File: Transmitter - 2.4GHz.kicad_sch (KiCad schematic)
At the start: 0 parts

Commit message: added RF ransceiver
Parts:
- added C19: 10uF 16V, 0_capacitors:CP_EIA-3216-18_Kemet-A, symbol 0_capacitors:TAJA106K016RNJ
- added C20: 100nF, 0_capacitors:C_0402_1005Metric, symbol 0_capacitors:CL05B104KO5NNNC
- added C21: 4.7uF, 0_capacitors:C_0805_2012Metric, symbol 0_capacitors:CL21A475KAQNNNE
- added E01-2G4M27D1: DS1023-2*4SF11, 0_modules:PE01-ML01DP5, symbol 0_modules:AFC07-S10ECC-00
- added R13, R14: 10kΩ, 0_resistors:R_0402_1005Metric, symbol 0_resistors:0402WGF1002TCE
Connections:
- new net +3.3V: C19.1, C20.1, C21.1, E01-2G4M27D1.2 (VCC), R13.2, R14.2
- new net GND: C19.2, C20.2, C21.2, E01-2G4M27D1.1 (GND)
- new net RF_CE: E01-2G4M27D1.3 (CE)
- new net RF_IRQ: E01-2G4M27D1.8 (IRQ), R14.1
- new net SPI5_MISO: E01-2G4M27D1.7 (MISO)
- new net SPI5_MOSI: E01-2G4M27D1.6 (MOSI)
- new net SPI5_NSS: E01-2G4M27D1.4 (CSN), R13.1
- new net SPI5_SCK: E01-2G4M27D1.5 (SCK)
- no-connect marks 0 -> 1

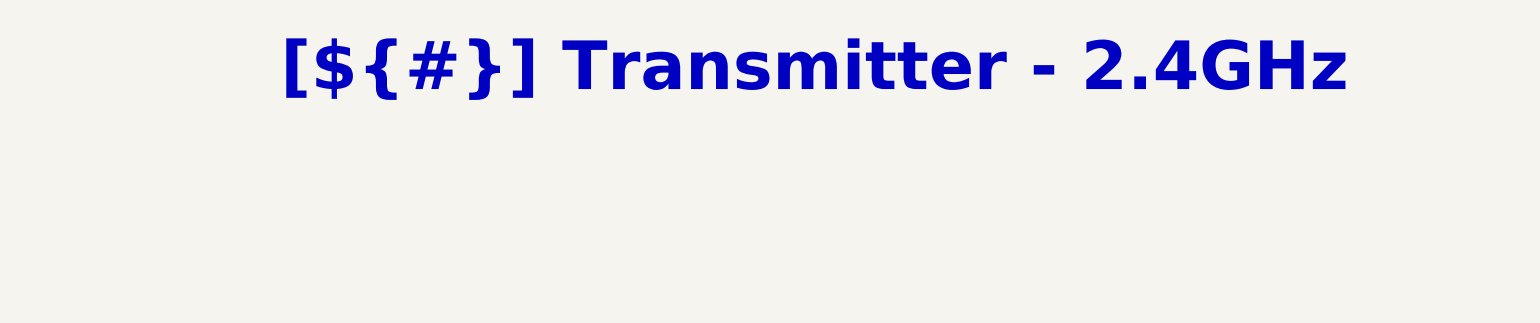
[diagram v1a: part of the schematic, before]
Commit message: added sd card schematic and refactor page numbers and general tab
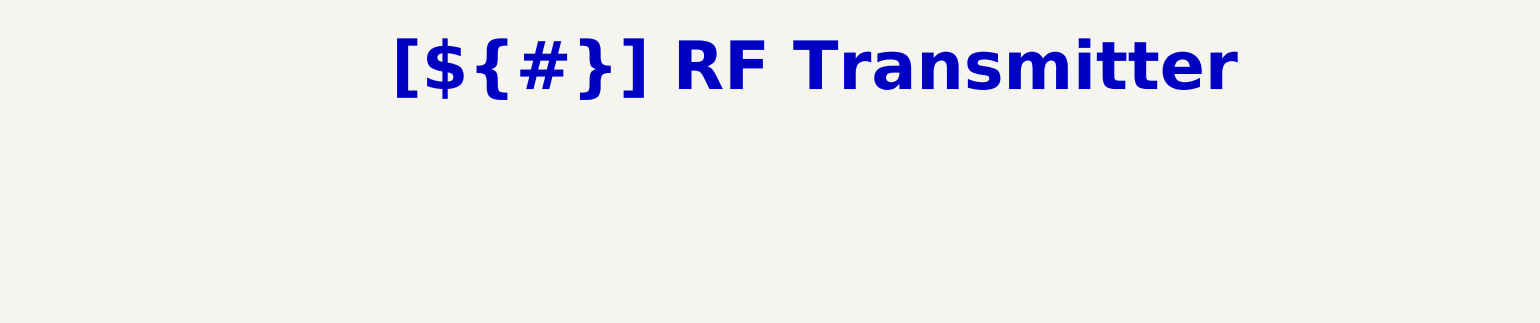
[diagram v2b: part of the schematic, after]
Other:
- title: Transmitter - 2.4GHz -> RF Transmitter
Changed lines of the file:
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@@
 	(paper "A3")
 	(title_block
-		(title "Transmitter - 2.4GHz")
+		(title "RF Transmitter")
 		(rev "${REVISION}")
 		(company "${COMPANY}")

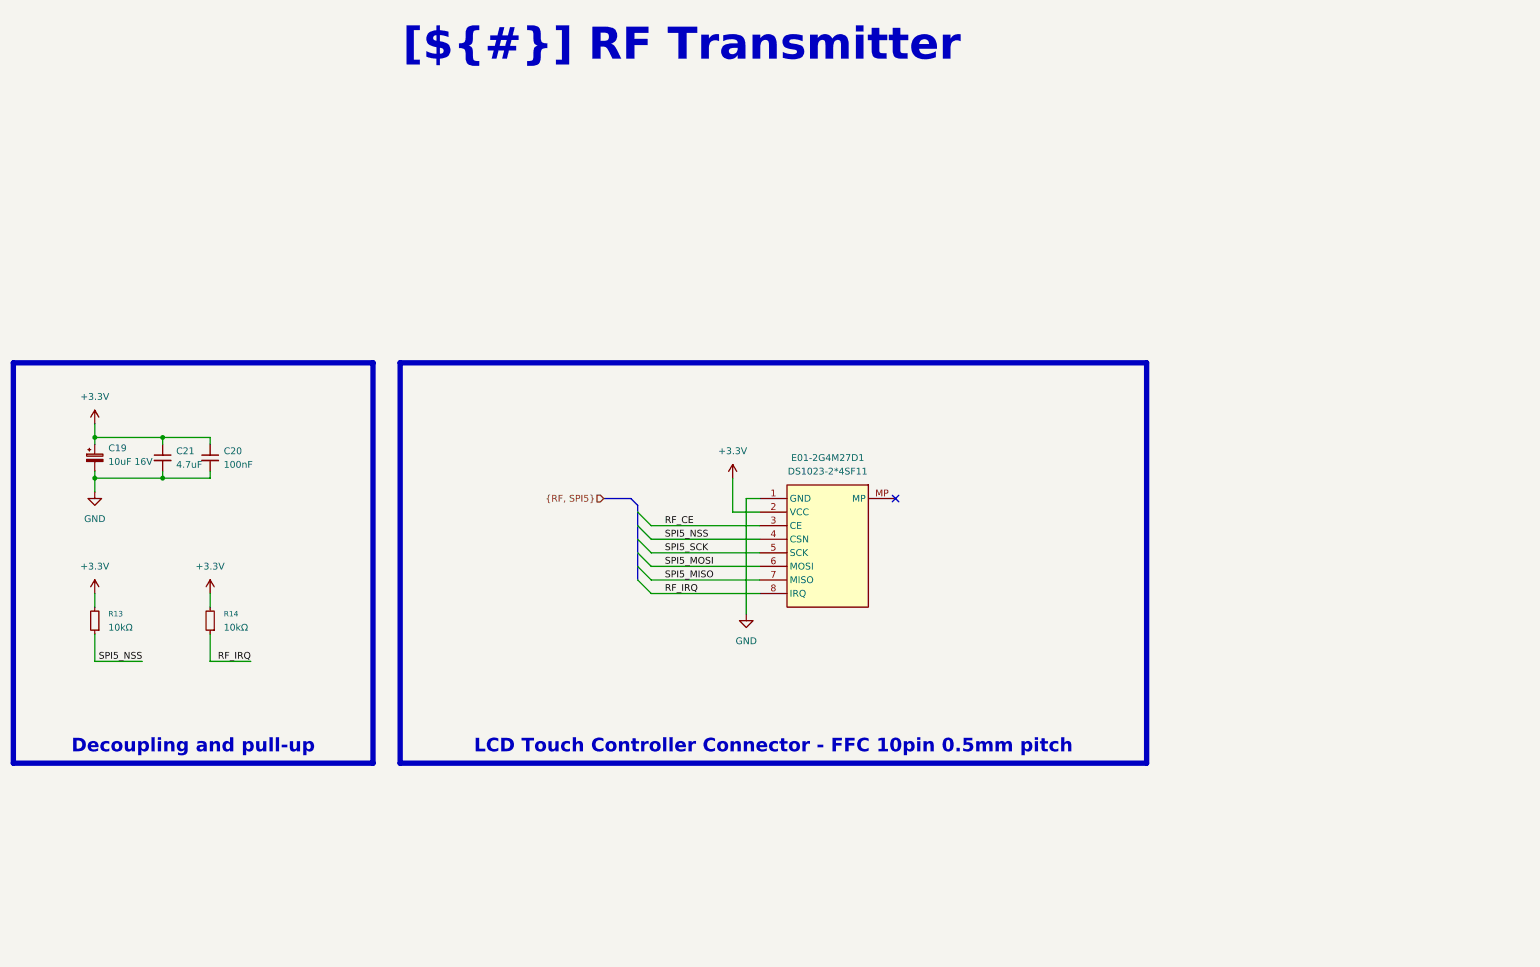
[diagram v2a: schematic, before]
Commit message: change the rf trasceiver and improve grounding near vias close to lcd connector
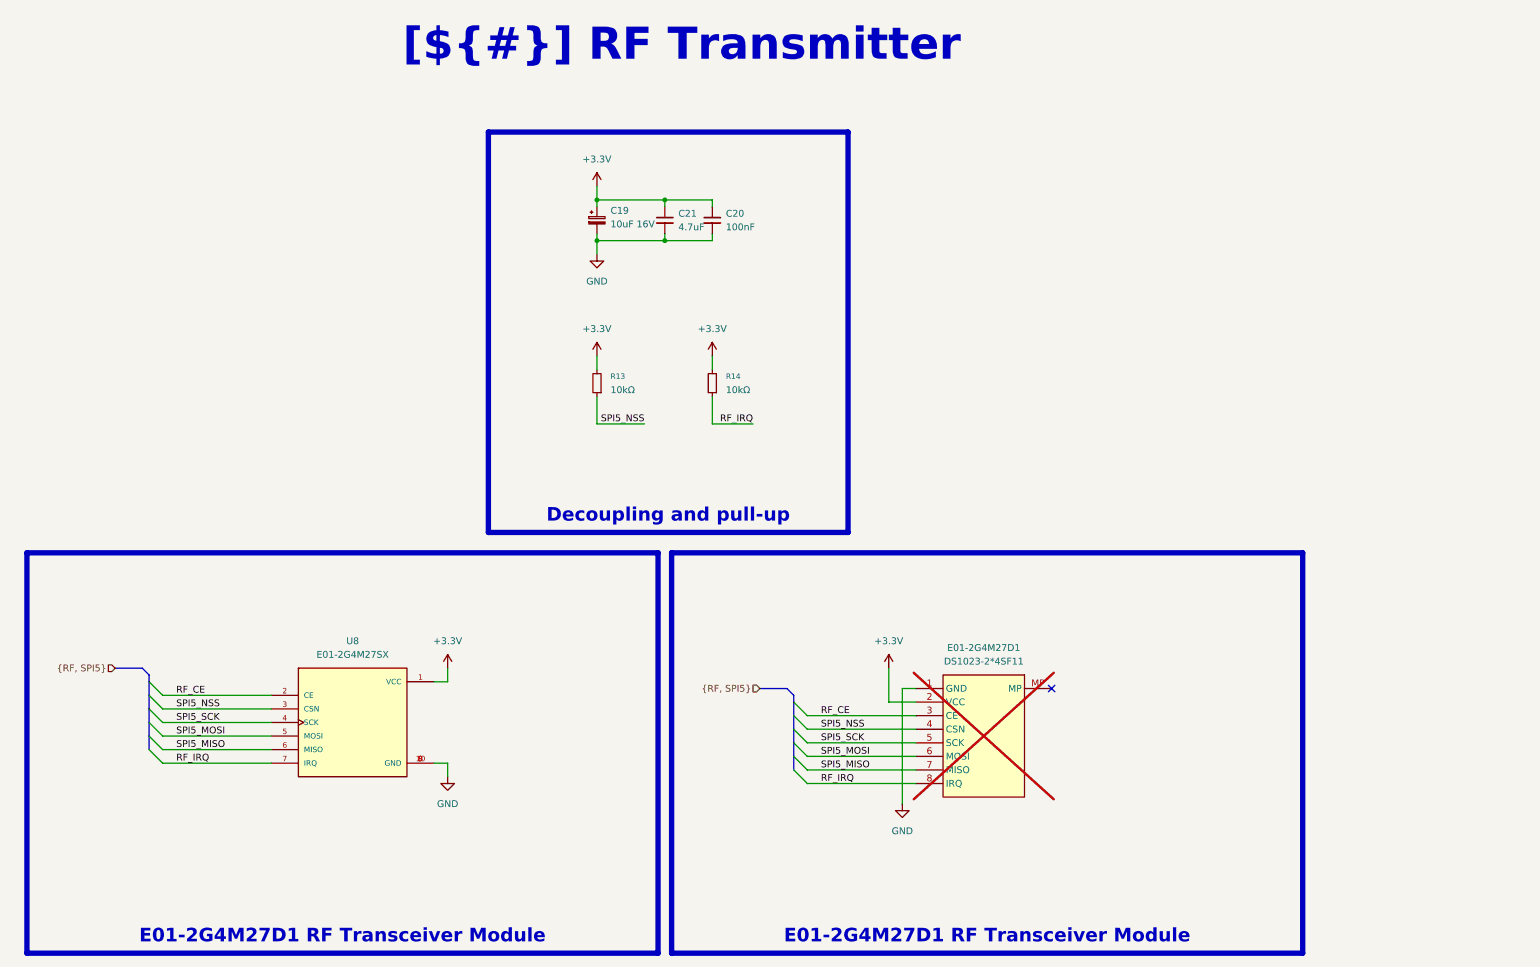
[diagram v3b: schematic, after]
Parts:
- added U8: E01-2G4M27SX, 0_modules:E01-2G4M27SX, symbol 0_modules:E01-2G4M27SX
- E01-2G4M27D1: now not fitted; now left out of the parts list
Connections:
- net +3.3V: now also U8.1 (VCC)
- net GND: now also U8.10 (GND), U8.8 (GND), U8.9 (GND)
- net RF_CE: now also U8.2 (CE)
- net RF_IRQ: now also U8.7 (IRQ)
- net SPI5_MISO: now also U8.6 (MISO)
- net SPI5_MOSI: now also U8.5 (MOSI)
- net SPI5_NSS: now also U8.3 (CSN)
- net SPI5_SCK: now also U8.4 (SCK)
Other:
- moved on the sheet: C19, C20, C21, R13, R14

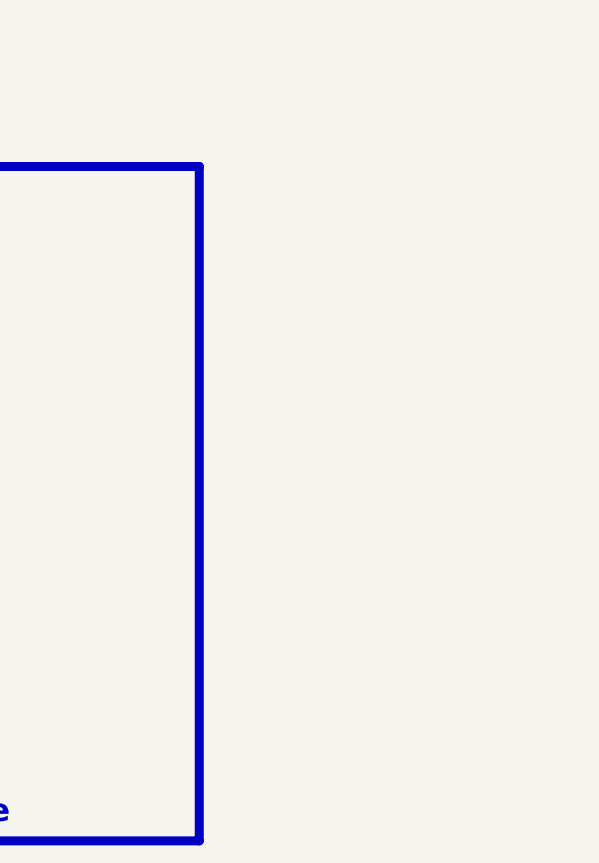
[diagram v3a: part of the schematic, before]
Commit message: added fiducal markers, mounting holes, testpoints
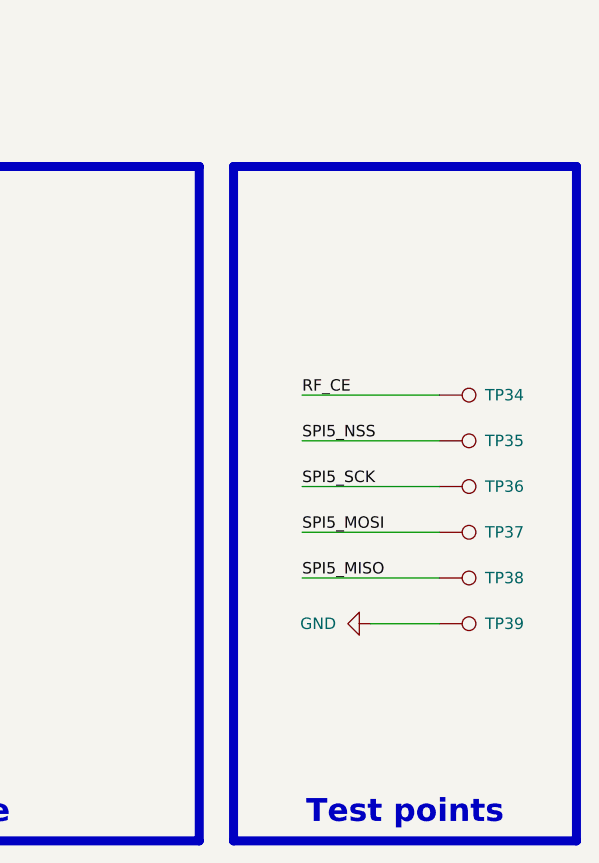
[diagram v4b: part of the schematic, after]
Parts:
- added TP34, TP35, TP36, TP37, TP38, TP39: TestPoint, 0_pads:TestPoint_Pad_D0.4mm_Back, symbol Connector:TestPoint
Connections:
- net GND: now also TP39.1
- net RF_CE: now also TP34.1
- net SPI5_MISO: now also TP38.1
- net SPI5_MOSI: now also TP37.1
- net SPI5_NSS: now also TP35.1
- net SPI5_SCK: now also TP36.1

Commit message: test points, colors, drc
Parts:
- TP34, TP35, TP36, TP37, TP38, TP39: footprint 0_pads:TestPoint_Pad_D0.4mm_Back -> 0_pads:TestPoint_Pad_D0.5mm_Back
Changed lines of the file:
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@@
 			)
 		)
-		(property "Footprint" "0_pads:TestPoint_Pad_D0.4mm_Back"
+		(property "Footprint" "0_pads:TestPoint_Pad_D0.5mm_Back"
 			(at 353.06 149.86 0)
 			(effects
@@
 			)
 		)
-		(property "Footprint" "0_pads:TestPoint_Pad_D0.4mm_Back"
+		(property "Footprint" "0_pads:TestPoint_Pad_D0.5mm_Back"
 			(at 353.06 144.78 0)
 			(effects
@@
 			)
 		)
-		(property "Footprint" "0_pads:TestPoint_Pad_D0.4mm_Back"
+		(property "Footprint" "0_pads:TestPoint_Pad_D0.5mm_Back"
 			(at 353.06 154.94 0)
 			(effects
@@
 			)
 		)
-		(property "Footprint" "0_pads:TestPoint_Pad_D0.4mm_Back"
+		(property "Footprint" "0_pads:TestPoint_Pad_D0.5mm_Back"
 			(at 353.06 170.18 0)
 			(effects
@@
 			)
 		)
-		(property "Footprint" "0_pads:TestPoint_Pad_D0.4mm_Back"
+		(property "Footprint" "0_pads:TestPoint_Pad_D0.5mm_Back"
 			(at 353.06 165.1 0)
 			(effects
@@
 			)
 		)
-		(property "Footprint" "0_pads:TestPoint_Pad_D0.4mm_Back"
+		(property "Footprint" "0_pads:TestPoint_Pad_D0.5mm_Back"
 			(at 353.06 160.02 0)
 			(effects

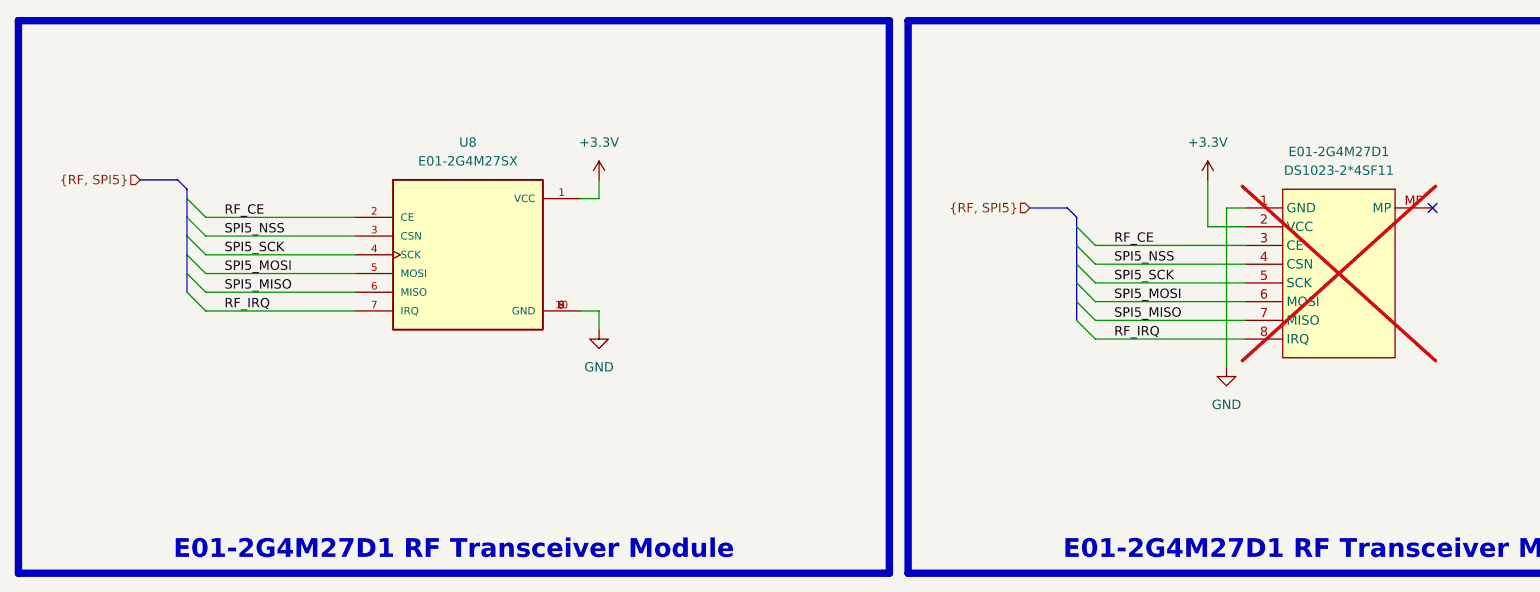
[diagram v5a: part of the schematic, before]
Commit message: designator chagnes and cleanup silkscreen
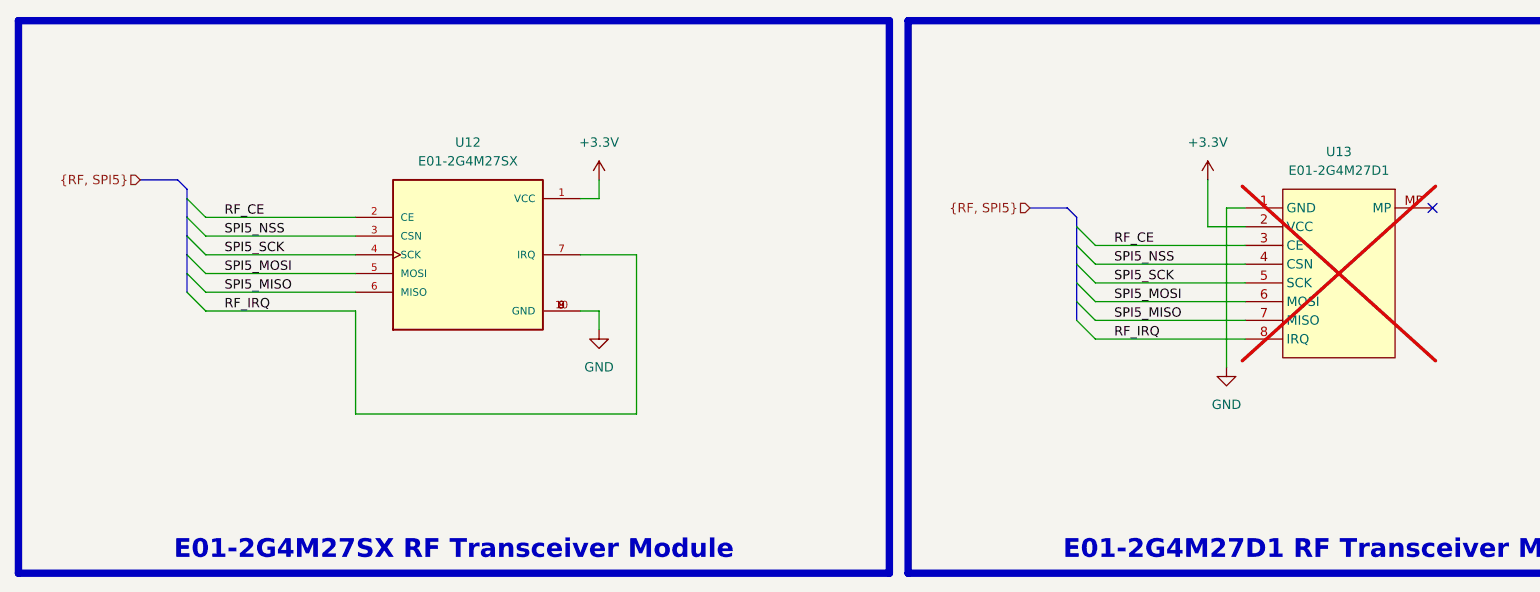
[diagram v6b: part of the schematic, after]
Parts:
- C19: LCSC PN (none) -> C7171
- C20: LCSC PN (none) -> C1525
- C21: LCSC PN (none) -> C1779
- R13, R14: LCSC PN (none) -> C25744
- U12: renamed from U8; LCSC PN (none) -> C2971733
- U13: renamed from E01-2G4M27D1; value DS1023-2*4SF11 -> E01-2G4M27D1
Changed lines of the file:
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@@
 		)
 	)
-	(text_box "E01-2G4M27D1 RF Transceiver Module"
+	(text_box "E01-2G4M27SX RF Transceiver Module"
 		(exclude_from_sim no)
 		(at 87.63 176.53 0)
@@
 		)
 	)
+	(wire
+		(pts
+			(xy 163.83 146.05) (xy 171.45 146.05)
+		)
+		(stroke
+			(width 0)
+			(type default)
+		)
+	)
 	(bus
 		(pts
@@
 		)
 	)
+	(wire
+		(pts
+			(xy 133.35 153.67) (xy 133.35 167.64)
+		)
+		(stroke
+			(width 0)
+			(type default)
+		)
+	)
 	(bus
 		(pts
@@
 	(wire
 		(pts
+			(xy 133.35 167.64) (xy 171.45 167.64)
+		)
+		(stroke
+			(width 0)
+			(type default)
+		)
+	)
+	(wire
+		(pts
 			(xy 233.68 144.78) (xy 254 144.78)
 		)
@@
 	(wire
 		(pts
+			(xy 171.45 146.05) (xy 171.45 167.64)
+		)
+		(stroke
+			(width 0)
+			(type default)
+		)
+	)
+	(wire
+		(pts
 			(xy 207.01 48.26) (xy 207.01 49.53)
 		)
@@
 			)
 		)
+		(property "LCSC PN" "C25744"
+			(at 194.31 82.55 0)
+			(effects
+				(font
+					(size 1.27 1.27)
+				)
+				(hide yes)
+			)
+		)
 		(pin "1"
 		)
@@
 		(dnp no)
 		(fields_autoplaced yes)
-		(property "Reference" "U8"
+		(property "Reference" "U12"
 			(at 148.59 130.81 0)
 			(effects
@@
 			)
 		)
+		(property "LCSC PN" "C2971733"
+			(at 148.59 146.05 0)
+			(effects
+				(font
+					(size 1.27 1.27)
+				)
+				(hide yes)
+			)
+		)
 		(pin "6"
 		)
@@
 			(project ""
 				(path "/0650c7a8-acba-429c-9f8e-eec0baf0bc1c/fede4c36-00cc-4d3d-b71c-5243ba232202/6d2d8335-c1d6-4f11-b5c7-265ea349210a"
-					(reference "U8")
+					(reference "U12")
 					(unit 1)
 				)
@@
 		(dnp yes)
 		(fields_autoplaced yes)
-		(property "Reference" "E01-2G4M27D1"
+		(property "Reference" "U13"
 			(at 266.7 132.08 0)
 			(effects
@@
 			)
 		)
-		(property "Value" "DS1023-2*4SF11"
+		(property "Value" "E01-2G4M27D1"
 			(at 266.7 134.62 0)
 			(effects
@@
 			(project ""
 				(path "/0650c7a8-acba-429c-9f8e-eec0baf0bc1c/fede4c36-00cc-4d3d-b71c-5243ba232202/6d2d8335-c1d6-4f11-b5c7-265ea349210a"
-					(reference "E01-2G4M27D1")
+					(reference "U13")
 					(unit 1)
 				)
@@
 			)
 		)
+		(property "LCSC PN" "C25744"
+			(at 215.9 82.55 0)
+			(effects
+				(font
+					(size 1.27 1.27)
+				)
+				(hide yes)
+			)
+		)
 		(pin "1"
 		)
@@
 			)
 		)
+		(property "LCSC PN" "C1525"
+			(at 215.9 52.07 0)
+			(effects
+				(font
+					(size 1.27 1.27)
+				)
+				(hide yes)
+			)
+		)
 		(pin "2"
 		)
@@
 			)
 		)
+		(property "LCSC PN" "C7171"
+			(at 194.31 52.07 0)
+			(effects
+				(font
+					(size 1.27 1.27)
+				)
+				(hide yes)
+			)
+		)
 		(pin "1"
 		)
@@
 			(at 207.01 52.07 0)
 			(effects
+				(font
+					(size 1.27 1.27)
+				)
+				(hide yes)
+			)
+		)
+		(property "LCSC PN" "C1779"
+			(at 207.01 52.07 0)
+			(effects
